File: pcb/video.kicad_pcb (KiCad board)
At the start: 4 copper layers, 159.9 x 99.9 mm, 163 parts, among them J1 09031966921, J3 Conn_02x07_Counter_Clockwise, J7 DB15_Female_HighDensity, J8 HDMI_A, U1 NCP115, U10 NCA9306DPH, U11 S62LV256AL-45TLI, U2 LP3853ESX-3.3/NOPB, U3 LCMXO2-1200HC-4TG100I, U4 LCMXO2-7000HC-4TG144C, U5 THS8136, U6 TFP410PAP, U7 ESD224DQA, U8 ESD224DQA, U9 PCA9540BDP, X1 ASV-xxxMHz

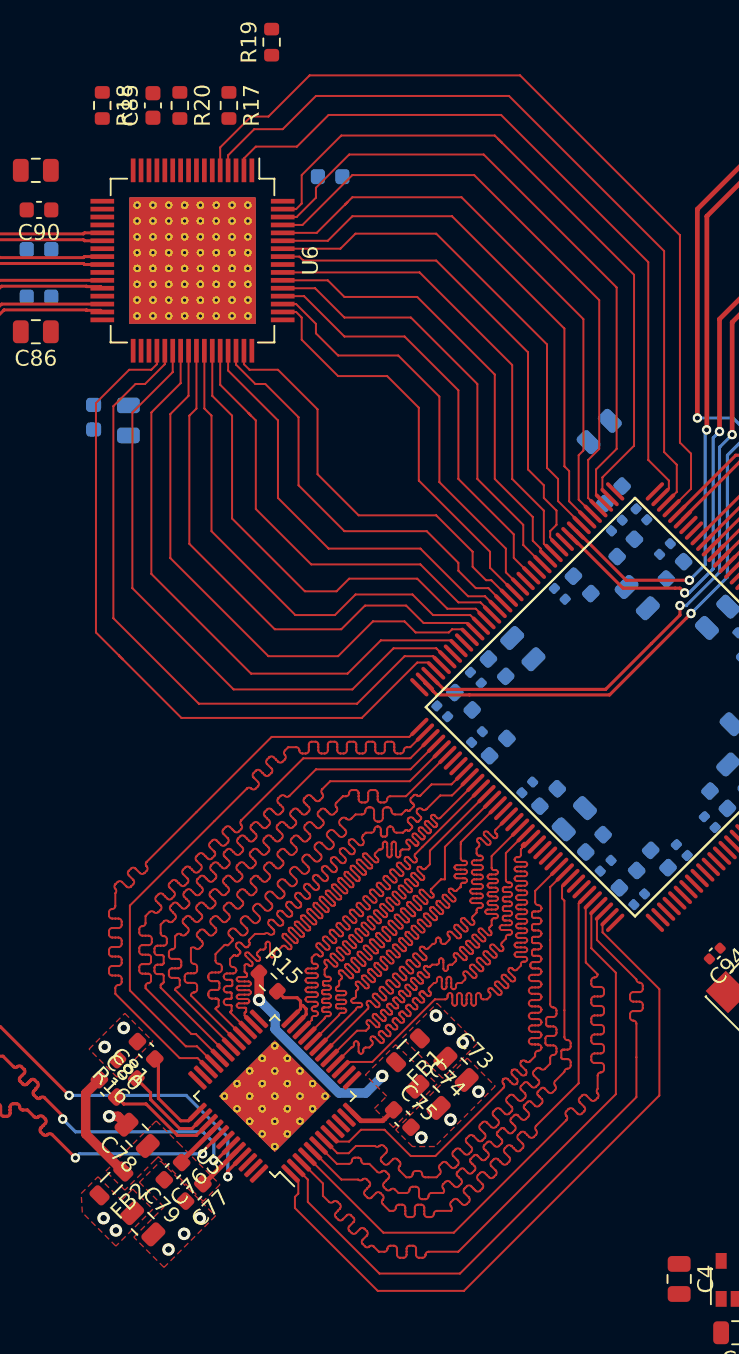
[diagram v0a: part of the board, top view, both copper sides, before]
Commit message: undo the trace length matching for the vga frontend
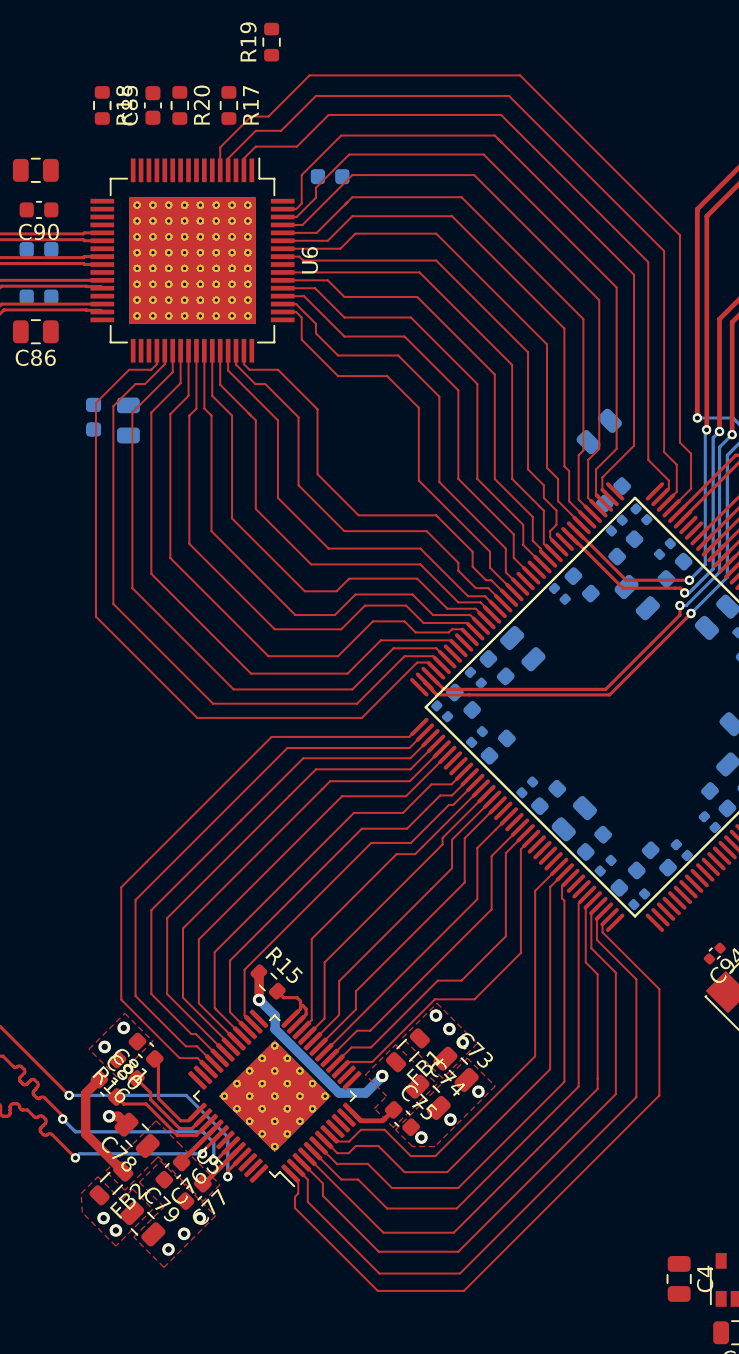
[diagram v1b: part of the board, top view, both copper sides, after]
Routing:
- net VGA_CLK: track 66.3 -> 23.2 mm
- net VGA_R3: track 44.5 -> 19.7 mm
- net VGA_R5: track 44.6 -> 19.9 mm
- net VGA_R6: track 44.6 -> 19.9 mm
- net VGA_R4: track 44.5 -> 19.9 mm
- net VGA_R2: track 44.5 -> 20.0 mm
- net VGA_R7: track 44.5 -> 20.6 mm
- net VGA_R1: track 44.5 -> 21.1 mm
- net VGA_R0: track 44.6 -> 21.9 mm
- net VGA_G7: track 44.5 -> 24.8 mm
- net VGA_G6: track 44.5 -> 26.5 mm
- net VGA_G5: track 44.6 -> 27.9 mm
- net VGA_B0: track 44.6 -> 29.4 mm
- net VGA_G4: track 44.7 -> 29.8 mm
- net VGA_B1: track 44.5 -> 31.0 mm
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
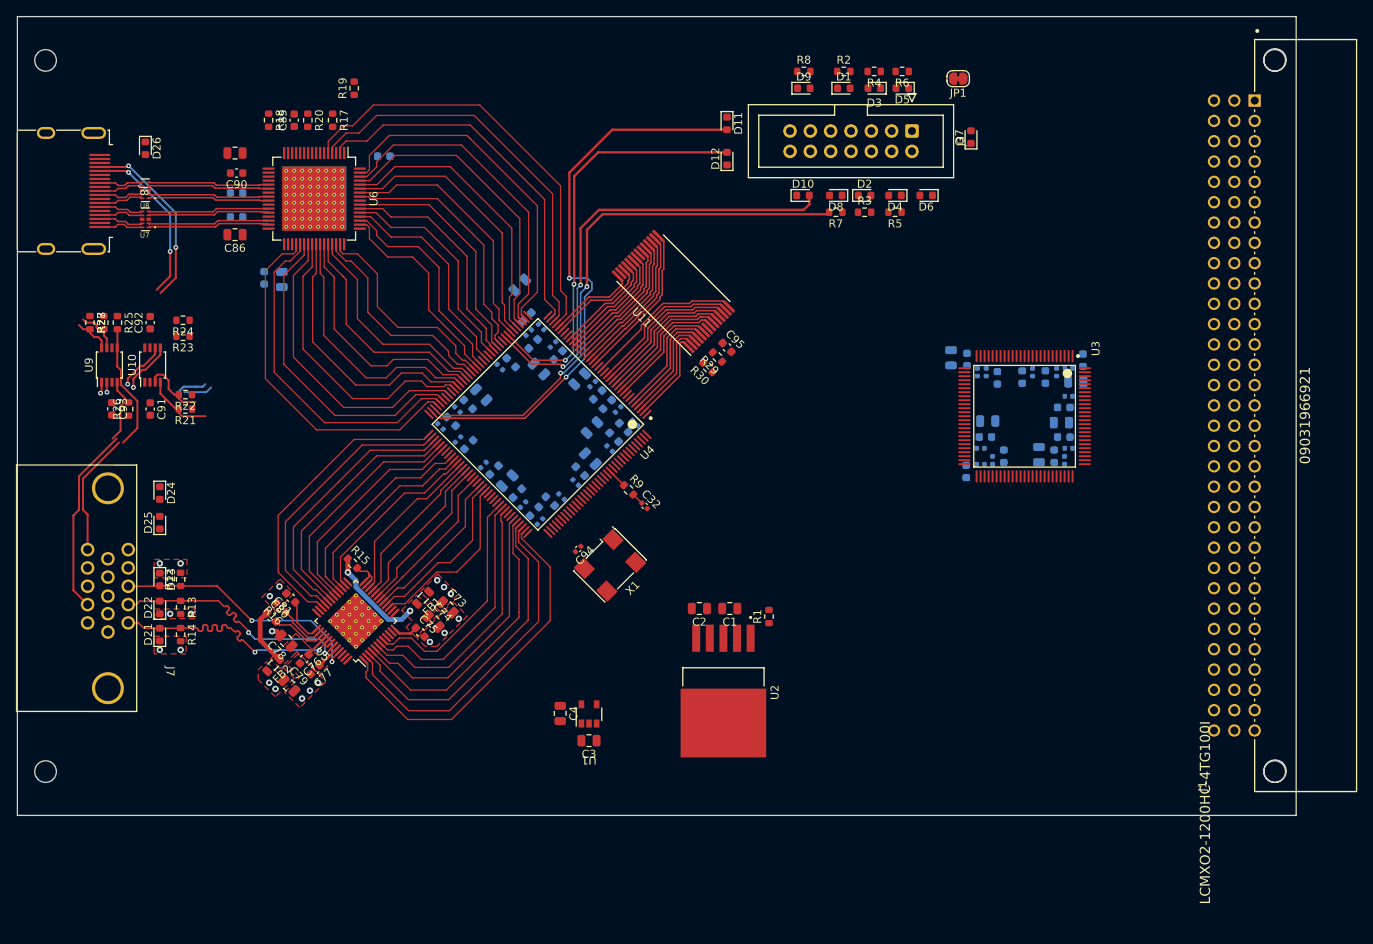
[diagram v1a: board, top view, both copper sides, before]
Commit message: add the 3v3 voltage regulator
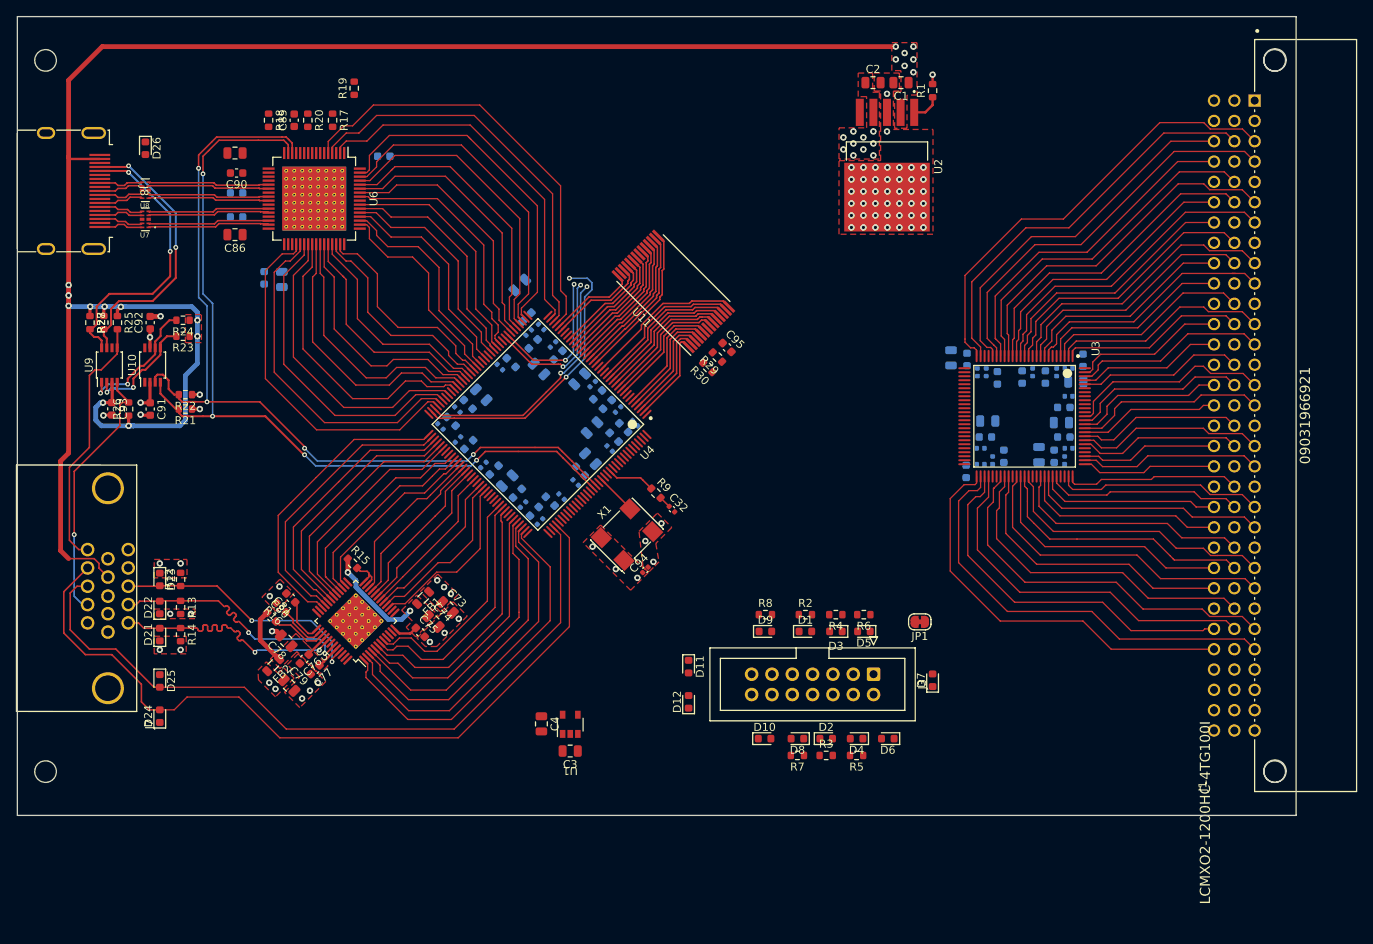
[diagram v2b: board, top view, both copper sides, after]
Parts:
- moved C2 69.2 mm to (162.0, 53.3), turned to 0 degrees
- moved C1 69.1 mm to (165.5, 53.3)
- moved R1 68.8 mm to (169.5, 54.3)
- moved U2 68.8 mm to (163.8, 67.6)
- moved D1 68.1 mm to (153.6, 121.9)
- moved D10 68.1 mm to (148.5, 135.3)
- moved D11 68.1 mm to (139.0, 126.3)
- moved D2 68.1 mm to (156.2, 135.3)
- moved D3 68.1 mm to (157.4, 121.9)
- moved D4 68.1 mm to (160.0, 135.3)
- moved D5 68.1 mm to (160.9, 121.9)
- moved D6 68.1 mm to (163.9, 135.3)
- moved D7 68.1 mm to (169.5, 128.0)
- moved D8 68.1 mm to (152.6, 135.3)
- moved D9 68.1 mm to (148.6, 121.9)
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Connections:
- C3 pad 1: +5V -> +3V3
- U1 pad 1: +5V -> +3V3
- U1 pad 3: +5V -> +3V3
- U3 pad 51: unconnected-(U3B-PR10D/(DQ1)) -> CONN_52
- U3 pad 52: unconnected-(U3B-PR10C/(DQ1)) -> CONN_51
- U3 pad 53: unconnected-(U3B-PR9D/(DQ1)) -> CONN_50
- U3 pad 54: CONN_52 -> CONN_49
- U3 pad 57: CONN_51 -> CONN_48
- U3 pad 58: CONN_50 -> CONN_47
- U3 pad 59: CONN_49 -> CONN_46
- U3 pad 60: CONN_48 -> unconnected-(U3B-PR8C/(DQ1))
- U3 pad 61: CONN_47 -> CONN_45
- U3 pad 62: CONN_46 -> CONN_44
- U3 pad 63: CONN_45 -> CONN_43
- U3 pad 64: CONN_44 -> CONN_42
- U3 pad 65: CONN_43 -> unconnected-(U3B-PR5A/(DQS0))
- U3 pad 66: CONN_42 -> unconnected-(U3B-PR4D/(DQ0))
- U4 pad 111: unconnected-(U4A-PT35B) -> VGA_HSYNC
- U4 pad 112: unconnected-(U4A-PT35A) -> VGA_VSYNC
- U4 pad 128: unconnected-(U4A-PT18A/PCLKT0_1) -> /Video FPGA/PLLIN
- U4 pad 94: (no net) -> unconnected-(U4B-PR11A/(DQS0))
- U4 pad 95: (no net) -> unconnected-(U4B-PR9B/(DQ0))
- U4 pad 96: (no net) -> unconnected-(U4B-PR9A/(DQ0))
- U4 pad 97: (no net) -> unconnected-(U4B-PR7B/(DQ0))
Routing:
- net +5V: track 0.00 -> 238.5 mm, vias 0 -> 19
- net FPGA_SCL: track 8.16 -> 109.6 mm, vias 0 -> 4
- net VGA_VSYNC: track 0.00 -> 99.8 mm
- net FPGA_SDA: track 8.50 -> 107.9 mm, vias 0 -> 4
- net VGA_HSYNC: track 0.00 -> 91.3 mm
- net CONN_0: track 0.00 -> 56.0 mm
- net CONN_51: track 0.00 -> 54.0 mm
- net CONN_52: track 0.00 -> 51.0 mm
- net CONN_1: track 0.00 -> 50.7 mm
- net CONN_3: track 0.00 -> 49.7 mm
- net CONN_48: track 0.00 -> 47.0 mm
- net CONN_2: track 0.00 -> 46.2 mm
- net CONN_49: track 0.00 -> 46.0 mm
- net CONN_50: track 0.00 -> 45.8 mm
- net CONN_6: track 0.00 -> 44.6 mm
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- added copper zone on F.Cu, net +5V
- added copper zone on In2.Cu, net +5V

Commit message: add the programming controller
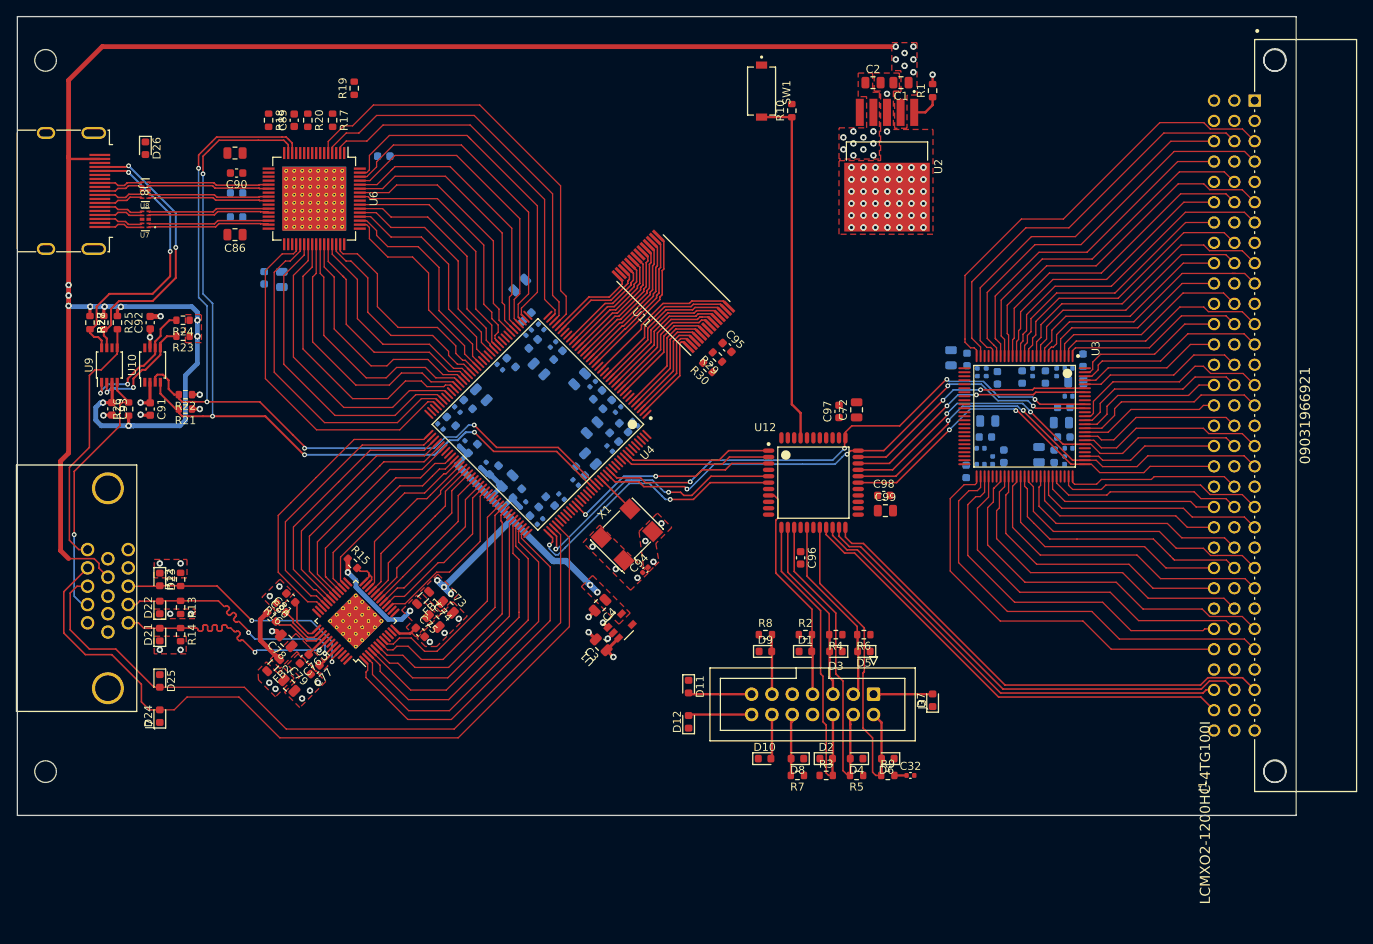
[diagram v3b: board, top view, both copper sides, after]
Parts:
- removed JP1: Jumper_2_Bridged, Jumper:SolderJumper-2_P1.3mm_Bridged_RoundedPad1.0x1.5mm
- added C72: 1u, Capacitor_SMD:C_0805_2012Metric, F.Cu at (160.0, 94.2)
- added C96: 100n, Capacitor_SMD:C_0603_1608Metric, F.Cu at (153.0, 112.7)
- added C97: 100n, Capacitor_SMD:C_0603_1608Metric, F.Cu at (157.8, 94.4)
- added C98: 100n, Capacitor_SMD:C_0603_1608Metric, F.Cu at (163.4, 104.9)
- added C99: 1u, Capacitor_SMD:C_0805_2012Metric, F.Cu at (163.6, 106.8)
- added R10: 10k, Resistor_SMD:R_0603_1608Metric, F.Cu at (151.9, 56.8)
- added SW1: SW_Push, PTS636_SM43J_SMTR_LFS:SW_PTS636_SM43J_SMTR_LFS, F.Cu at (148.1, 54.4)
- added U12: XC9572XL-10VQG44C, XC9572XL-10VQG44C:Xilinx-XC9572XL-10VQG44C-Level_C, F.Cu at (154.6, 103.3)
- moved R9 45.7 mm to (163.9, 139.9), turned to 0 degrees
- moved C32 44.7 mm to (166.7, 139.9), turned to 0 degrees
- moved C4 16.5 mm to (127.9, 118.7), turned to -135 degrees
- moved C3 13.8 mm to (128.1, 123.6), turned to 135 degrees
- moved U1 13.7 mm to (129.6, 122.1), turned to 135 degrees
- moved D11 2.50 mm to (139.0, 128.8)
- moved D1 2.50 mm to (153.6, 124.4)
- moved D10 2.50 mm to (148.5, 137.8)
- moved D12 2.50 mm to (139.0, 133.2)
- moved D2 2.50 mm to (156.2, 137.8)
- moved D3 2.50 mm to (157.4, 124.4)
- moved D4 2.50 mm to (160.0, 137.8)
- moved D5 2.50 mm to (160.9, 124.4)
- moved D6 2.50 mm to (163.9, 137.8)
- moved D7 2.50 mm to (169.5, 130.5)
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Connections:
- D1 pad 2: JTAG_TMS -> JTAG_TMS_IN
- D2 pad 2: VIDEO_CTRL_TDO -> VIDEO_CTRL_TDO_IN
- D3 pad 2: VIDEO_CTRL_TDI -> VIDEO_CTRL_TDI_IN
- D4 pad 2: BUS_CTRL_TDO -> BUS_CTRL_TDO_IN
- D5 pad 2: BUS_CTRL_TDI -> BUS_CTRL_TDI_IN
- D6 pad 2: JTAG_TCK -> JTAG_TCK_IN
- J1 pad 3: unconnected-(J1-Pad3) -> RESET_CONN
- J1 pad 88: unconnected-(J1-Pad88) -> TMS_CONN
- J1 pad 89: unconnected-(J1-Pad89) -> TCK_CONN
- J1 pad 90: GND -> TDI_CONN
- J1 pad 93: GND -> TDO_CONN
- J3 pad 2: JTAG_TCK -> JTAG_TCK_IN
- J3 pad 3: BUS_CTRL_TDI -> BUS_CTRL_TDI_IN
- J3 pad 4: BUS_CTRL_TDO -> BUS_CTRL_TDO_IN
- J3 pad 5: VIDEO_CTRL_TDI -> VIDEO_CTRL_TDI_IN
- J3 pad 6: VIDEO_CTRL_TDO -> VIDEO_CTRL_TDO_IN
- J3 pad 7: JTAG_TMS -> JTAG_TMS_IN
- R2 pad 2: JTAG_TMS -> JTAG_TMS_IN
- R3 pad 2: VIDEO_CTRL_TDO -> VIDEO_CTRL_TDO_IN
- R4 pad 2: VIDEO_CTRL_TDI -> VIDEO_CTRL_TDI_IN
- R5 pad 2: BUS_CTRL_TDO -> BUS_CTRL_TDO_IN
- R6 pad 2: BUS_CTRL_TDI -> BUS_CTRL_TDI_IN
- R9 pad 1: JTAG_TCK -> JTAG_TCK_IN
- U3 pad 76: CONN_34 -> BUS_DONE
- U3 pad 77: CONN_33 -> BUS_INITB
- U3 pad 78: CONN_32 -> CONN_31
- U3 pad 81: CONN_31 -> BUS_PROGB
- U4 pad 109: unconnected-(U4A-PT36D/DONE) -> VIDEO_DONE
- U4 pad 110: unconnected-(U4A-PT36C/INITN) -> VIDEO_INITB
- U4 pad 119: unconnected-(U4A-PT27D/PROGRAMN) -> VIDEO_PROGB
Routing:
- net JTAG_TMS: track 0.00 -> 67.2 mm, vias 0 -> 4
- net JTAG_TCK: track 6.06 -> 67.7 mm, vias 0 -> 4
- net TMS_CONN: track 0.00 -> 61.0 mm
- net TCK_CONN: track 0.00 -> 59.3 mm
- net TDO_CONN: track 0.00 -> 58.5 mm
- net BUS_INITB: track 0.00 -> 57.7 mm, vias 0 -> 2
- net TDI_CONN: track 0.00 -> 57.0 mm
- net BUS_PROGB: track 0.00 -> 54.4 mm, vias 0 -> 2
- net BUS_DONE: track 0.00 -> 51.9 mm, vias 0 -> 2
- net +1V8: track 0.00 -> 51.4 mm, vias 3 -> 5
- net RESET: track 0.00 -> 44.3 mm
- net JTAG_TCK_IN: track 0.00 -> 42.7 mm
- net BUS_CTRL_TDO_IN: track 0.00 -> 41.8 mm
- net VIDEO_CTRL_TDO_IN: track 0.00 -> 41.6 mm
- net VIDEO_DONE: track 0.00 -> 35.5 mm, vias 0 -> 2
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- added copper zone on In2.Cu, net +3V3
